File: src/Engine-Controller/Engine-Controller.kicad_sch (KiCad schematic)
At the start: 16 parts, among them J2 Jumper_NO, P3 SBH11-PBPC-D10-RA-BK, U1 STM32H750VBTx

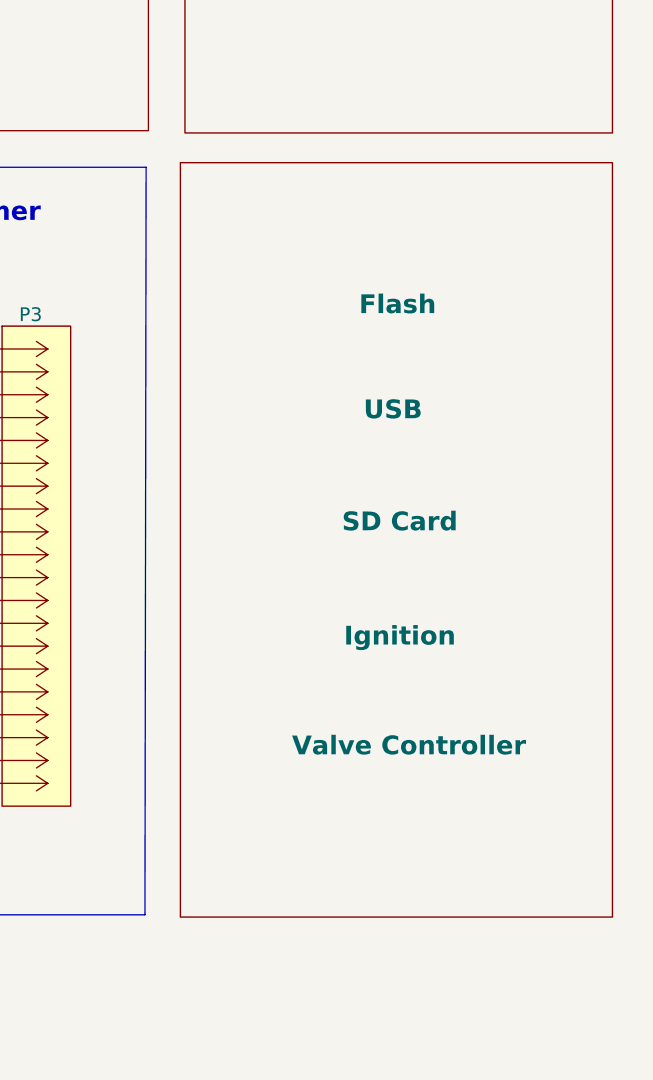
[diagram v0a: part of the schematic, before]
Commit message: added crystal oscillator to schematic
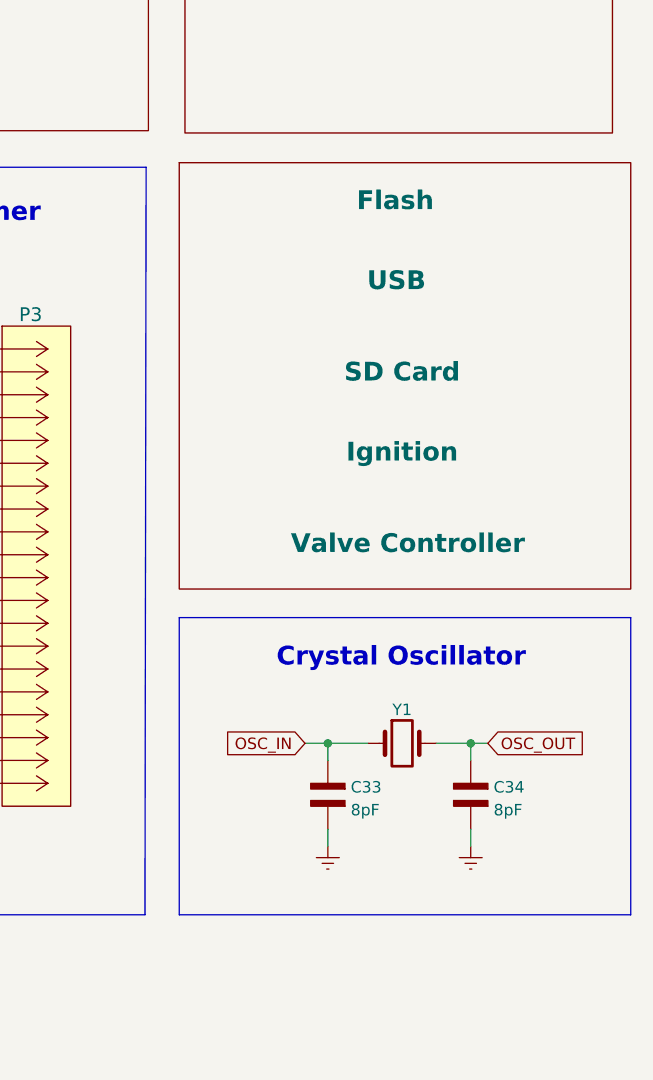
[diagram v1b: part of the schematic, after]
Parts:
- added C33, C34: 8pF, symbol Engine-Controller:CAP_0603
- added Y1: ECS-240-18-33-JGN-TR, symbol Engine-Controller:ECS-240-18-33-JGN-TR
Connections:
- net Earth: now also C33.2, C34.2
- net OSC_IN: now also C33.1, Y1.1
- net OSC_OUT: now also C34.1, Y1.3
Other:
- note added: "Crystal Oscillator"

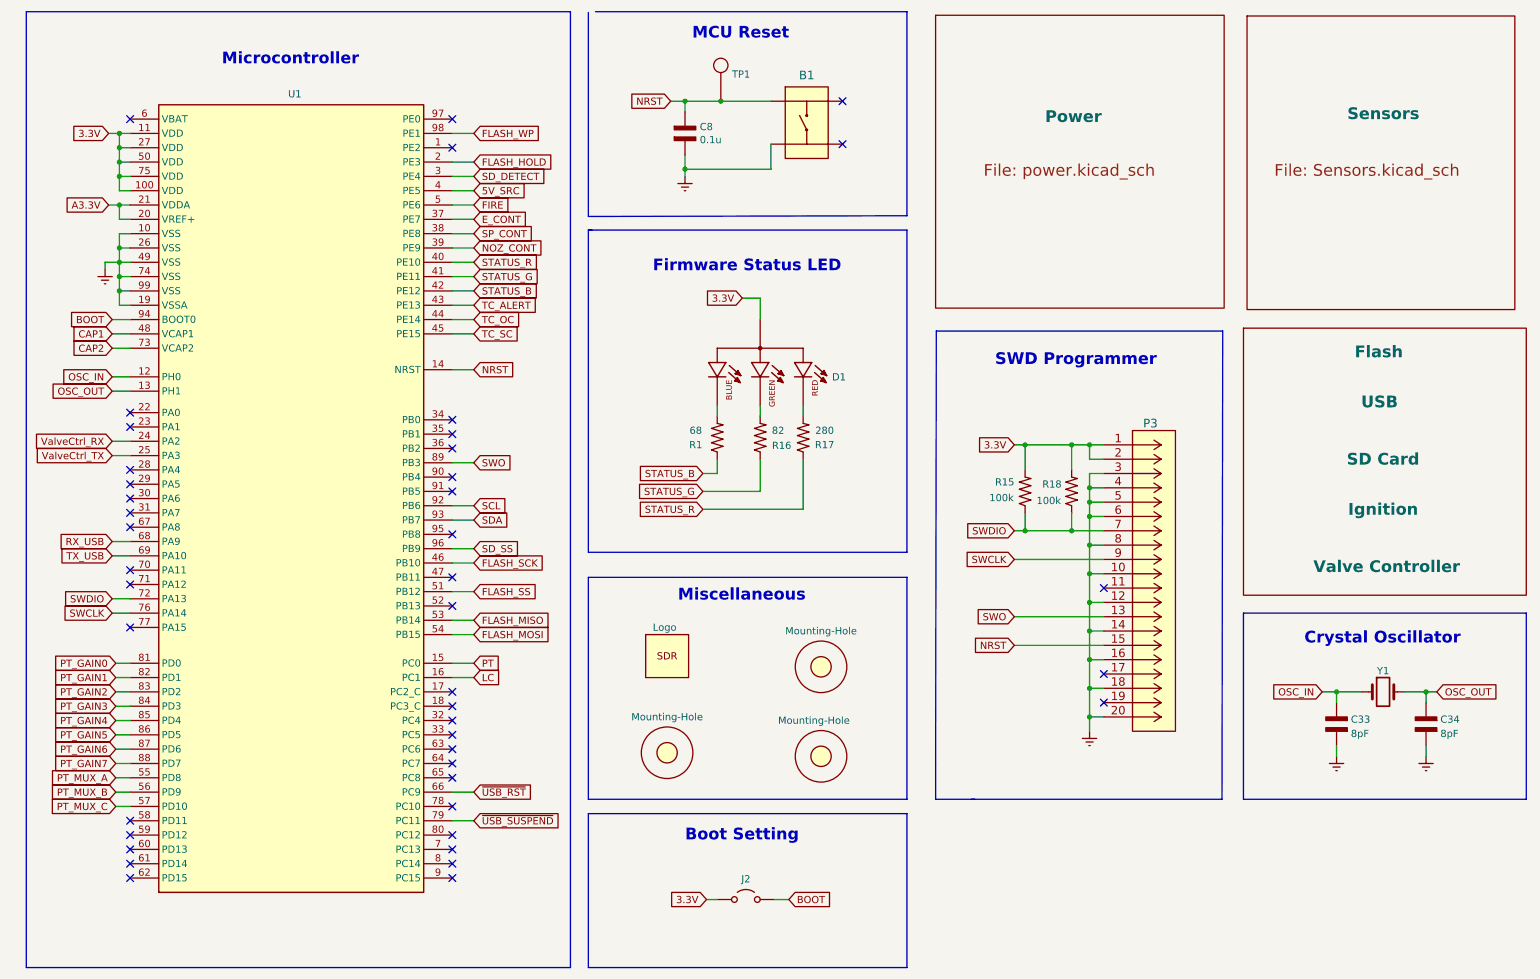
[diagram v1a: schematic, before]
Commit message: added wireless interface to schematic
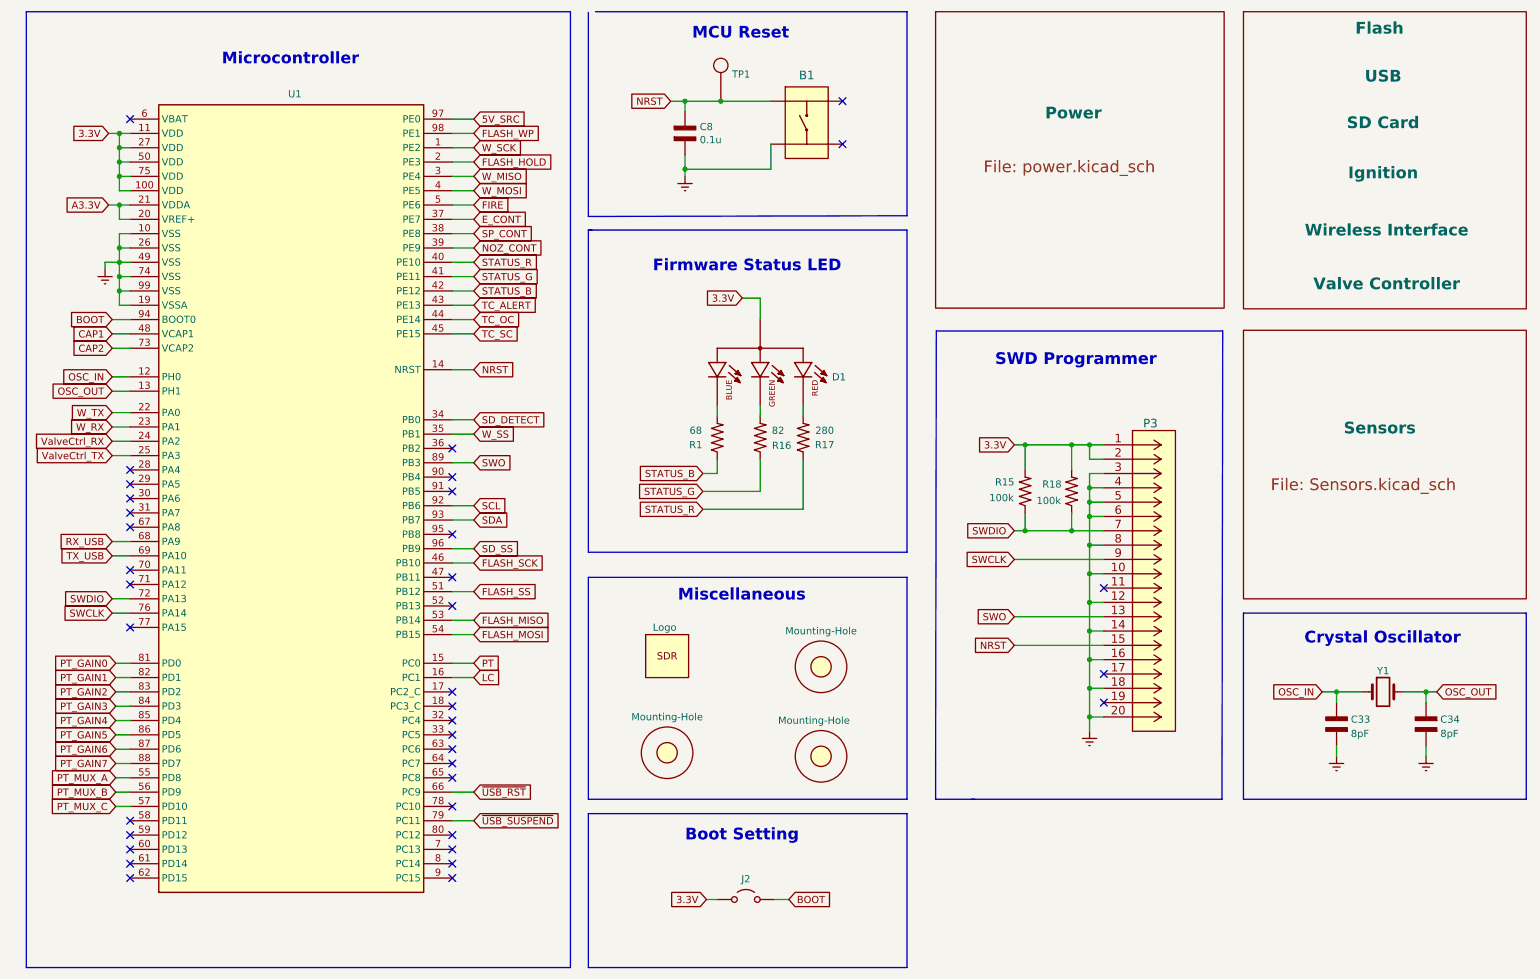
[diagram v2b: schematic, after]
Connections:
- net 5V_SRC: now also U1.97 (PE0); no longer U1.4 (PE5)
- net SD_DETECT: now also U1.34 (PB0); no longer U1.3 (PE4)
- net W_SCK: now reaches U1.1 (PE2)
- net W_TX: now reaches U1.22 (PA0)
- net W_RX: now reaches U1.23 (PA1)
- net W_SS: now reaches U1.35 (PB1)
- new net W_MISO: U1.3 (PE4)
- new net W_MOSI: U1.4 (PE5)
- no-connect marks 43 -> 37

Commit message: resolved all ERC schematic issues
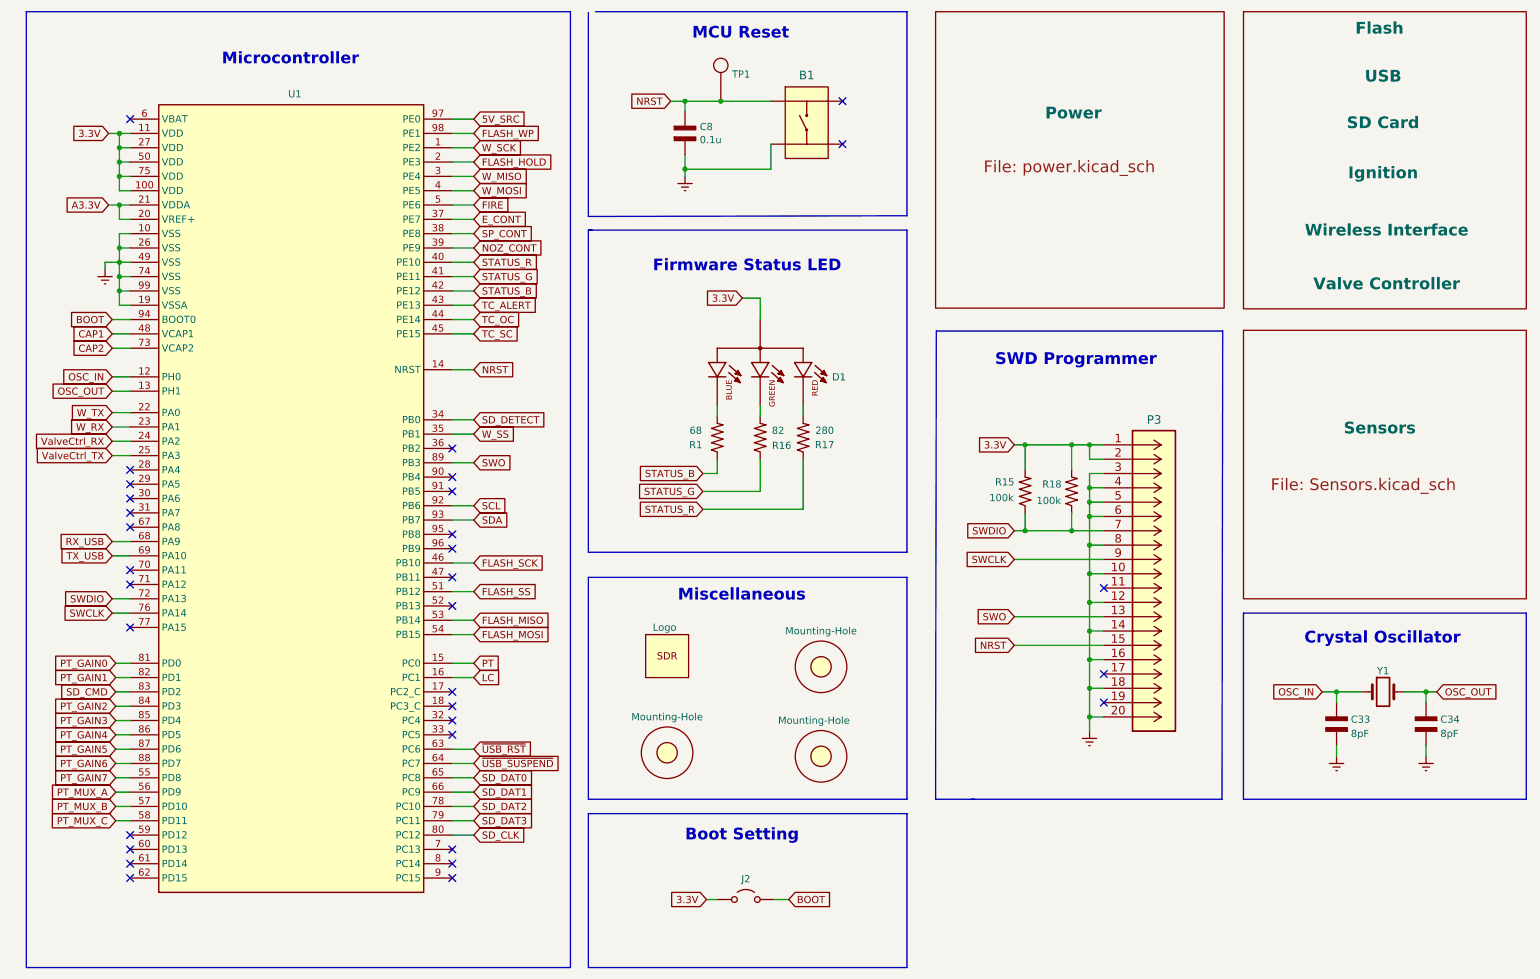
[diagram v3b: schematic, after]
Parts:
- removed P3: SBH11-PBPC-D10-RA-BK, CONN20_D10-RA-BK_SUL, symbol Engine-Controller:SBH11-PBPC-D10-RA-BK
- added P3: 3220-20-0200-00, Engine-Controller:3220-20-0200-00, symbol Engine-Controller:3220-20-0200-00
- B1: footprint SW_PTS647SM38SMTR2LFS_CNK -> Engine-Controller:PTS647SM38SMTR2LFS
- C33, C34: footprint (none) -> Engine-Controller:CAP_0603
- D1: footprint LED_CLMVC-FKA-CL1D1L71BB7C3C3 -> Engine-Controller:CLMVC-FKA-CL1D1L71BB7C3C3
- R1, R15, R16, R17, R18: footprint (none) -> Engine-Controller:RES_0603
- U1: footprint Engine-Controller:STM32H750VBT6 -> Package_QFP:LQFP-100_14x14mm_P0.5mm
- Y1: footprint (none) -> Engine-Controller:ECS-240-18-33-JGN-TR
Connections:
- net 3.3V: now also P3.1, P3.2
- net Earth: now also P3.10, P3.12, P3.14, P3.16, P3.18, P3.20, P3.3, P3.4, P3.5, P3.6, P3.8
- net NRST: now also P3.15
- net PT_GAIN2: now also U1.84 (PD3); no longer U1.83 (PD2)
- net PT_GAIN3: now also U1.85 (PD4); no longer U1.84 (PD3)
- net PT_GAIN4: now also U1.86 (PD5); no longer U1.85 (PD4)
- net PT_GAIN5: now also U1.87 (PD6); no longer U1.86 (PD5)
- net PT_GAIN6: now also U1.88 (PD7); no longer U1.87 (PD6)
- net PT_GAIN7: now also U1.55 (PD8); no longer U1.88 (PD7)
- net PT_MUX_A: now also U1.56 (PD9); no longer U1.55 (PD8)
- net PT_MUX_B: now also U1.57 (PD10); no longer U1.56 (PD9)
- net PT_MUX_C: now also U1.58 (PD11); no longer U1.57 (PD10)
- net SWCLK: now also P3.9
- net SWDIO: now also P3.7
- net SWO: now also P3.13
- net ~{USB_RST}: now also U1.63 (PC6); no longer U1.66 (PC9)
- net ~{USB_SUSPEND}: now also U1.64 (PC7); no longer U1.79 (PC11)
- net SD_DAT0: now reaches U1.65 (PC8)
- net SD_DAT2: now reaches U1.78 (PC10)
- net SD_CLK: now reaches U1.80 (PC12)
- net SD_SS: no longer names the net of U1.96 (PB9)
- new net SD_CMD: U1.83 (PD2)
- new net SD_DAT1: U1.66 (PC9)
- new net SD_DAT3: U1.79 (PC11)
- no-connect marks 37 -> 32

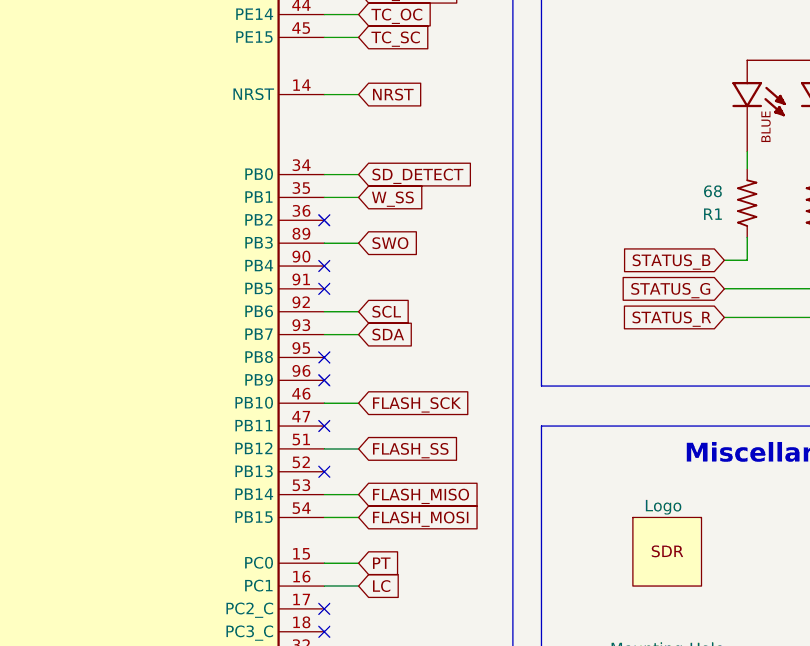
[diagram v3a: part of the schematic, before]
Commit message: removed unused traces in layout
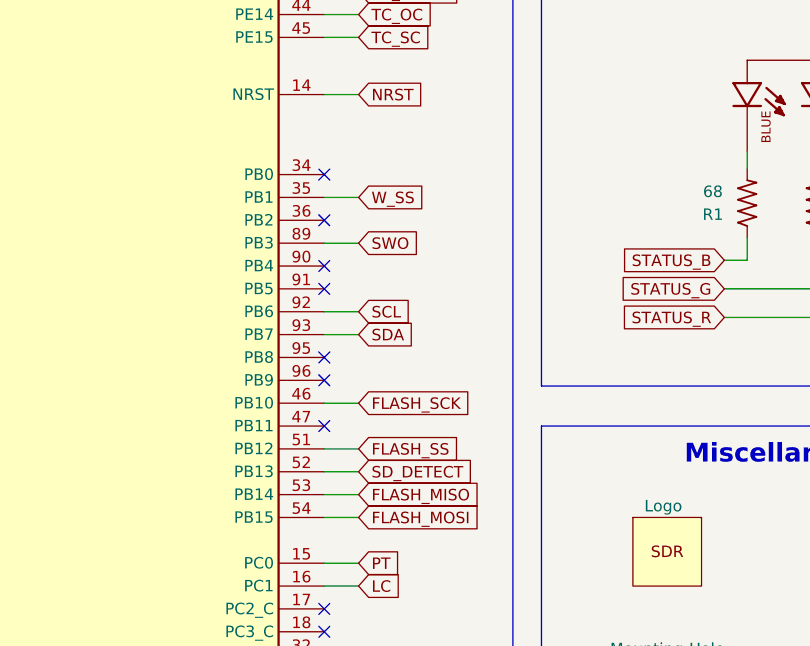
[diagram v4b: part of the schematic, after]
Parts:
- U1: footprint Package_QFP:LQFP-100_14x14mm_P0.5mm -> Engine-Controller:STM32H750VBT6
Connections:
- net SD_DETECT: now also U1.52 (PB13); no longer U1.34 (PB0)
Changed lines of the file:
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@@
   (no_connect (at 34.29 173.99))
   (no_connect (at 91.44 173.99))
-  (no_connect (at 91.44 125.73))
   (no_connect (at 34.29 119.38))
+  (no_connect (at 91.44 92.71))
   (no_connect (at 34.29 129.54))
   (no_connect (at 91.44 143.51))
@@
     (stroke (width 0) (type default) (color 0 0 0 0))
   )
-  (wire (pts (xy 91.44 92.71) (xy 95.25 92.71))
-    (stroke (width 0) (type default) (color 0 0 0 0))
-  )
   (wire (pts (xy 204.47 130.175) (xy 204.47 125.095))
     (stroke (width 0) (type default) (color 0 0 0 0))
@@
   )
   (polyline (pts (xy 15.875 20.32) (xy 15.875 189.865))
+    (stroke (width 0) (type default) (color 0 0 0 0))
+  )
+  (wire (pts (xy 91.44 125.73) (xy 95.25 125.73))
     (stroke (width 0) (type default) (color 0 0 0 0))
   )
@@
     )
   )
-  (global_label "SD_DETECT" (shape input) (at 95.25 92.71 0) (fields_autoplaced)
-    (effects (font (size 1.27 1.27)) (justify left))
-    (property "Intersheet References" "${INTERSHEET_REFS}" (id 0) (at -43.18 48.26 0)
+  (global_label "SD_DETECT" (shape input) (at 95.25 125.73 0) (fields_autoplaced)
+    (effects (font (size 1.27 1.27)) (justify left))
+    (property "Intersheet References" "${INTERSHEET_REFS}" (id 0) (at -43.18 81.28 0)
       (effects (font (size 1.27 1.27)) hide)
     )
@@
       (effects (font (size 1.27 1.27)) hide)
     )
-    (property "Footprint" "Package_QFP:LQFP-100_14x14mm_P0.5mm" (id 2) (at 45.72 176.53 0)
+    (property "Footprint" "Engine-Controller:STM32H750VBT6" (id 2) (at 45.72 176.53 0)
       (effects (font (size 1.27 1.27)) (justify right) hide)
     )
@@
     )
     (path "/00000000-0000-0000-0000-0000614b51f2"
-      (reference "U1") (unit 1) (value "STM32H750VBTx") (footprint "Package_QFP:LQFP-100_14x14mm_P0.5mm")
+      (reference "U1") (unit 1) (value "STM32H750VBTx") (footprint "Engine-Controller:STM32H750VBT6")
     )
     (path "/00000000-0000-0000-0000-000060d7f309/00000000-0000-0000-0000-0000611b83f2"
